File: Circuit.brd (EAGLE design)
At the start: 99 x 72.1 mm, 115 parts, among them IC1 LM1117T-3.3-V, P1 RASPI-P1RASPI_REV2_P1, P5 RASPI_P5

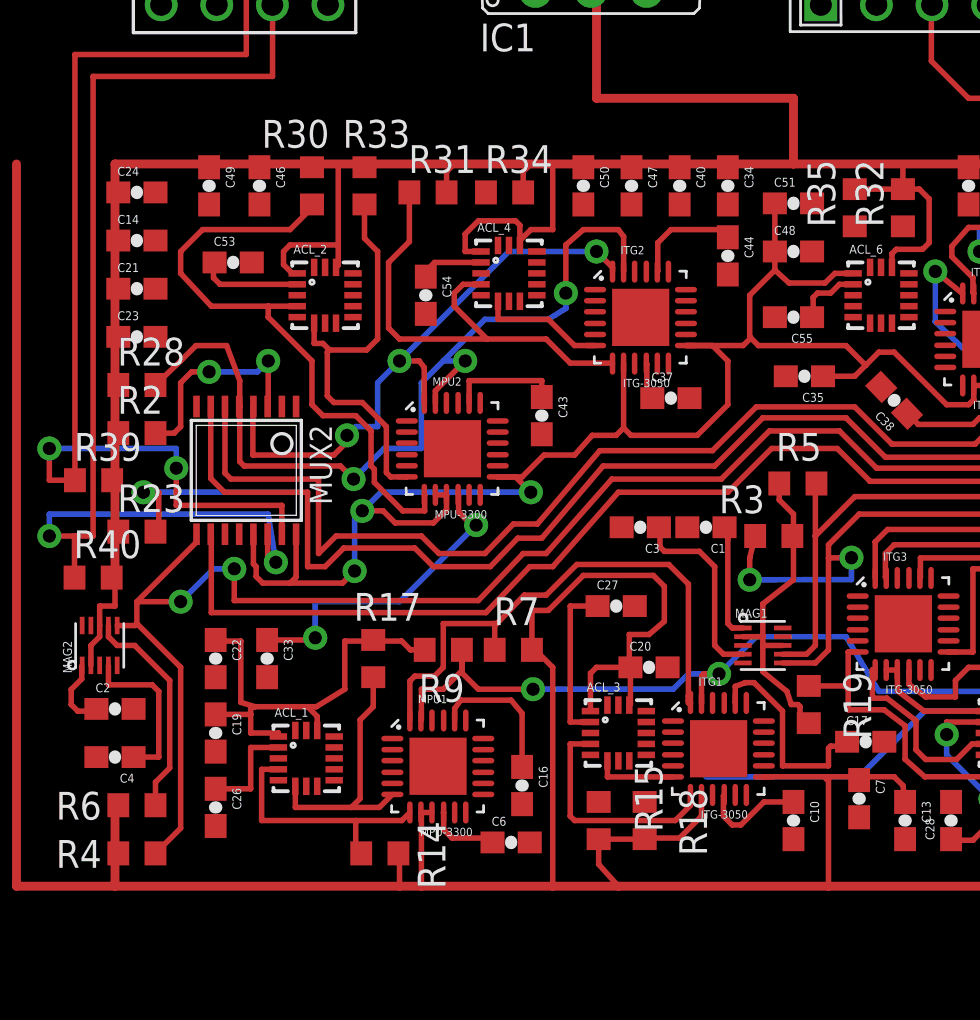
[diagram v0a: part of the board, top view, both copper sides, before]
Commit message: Sorting out missing connections
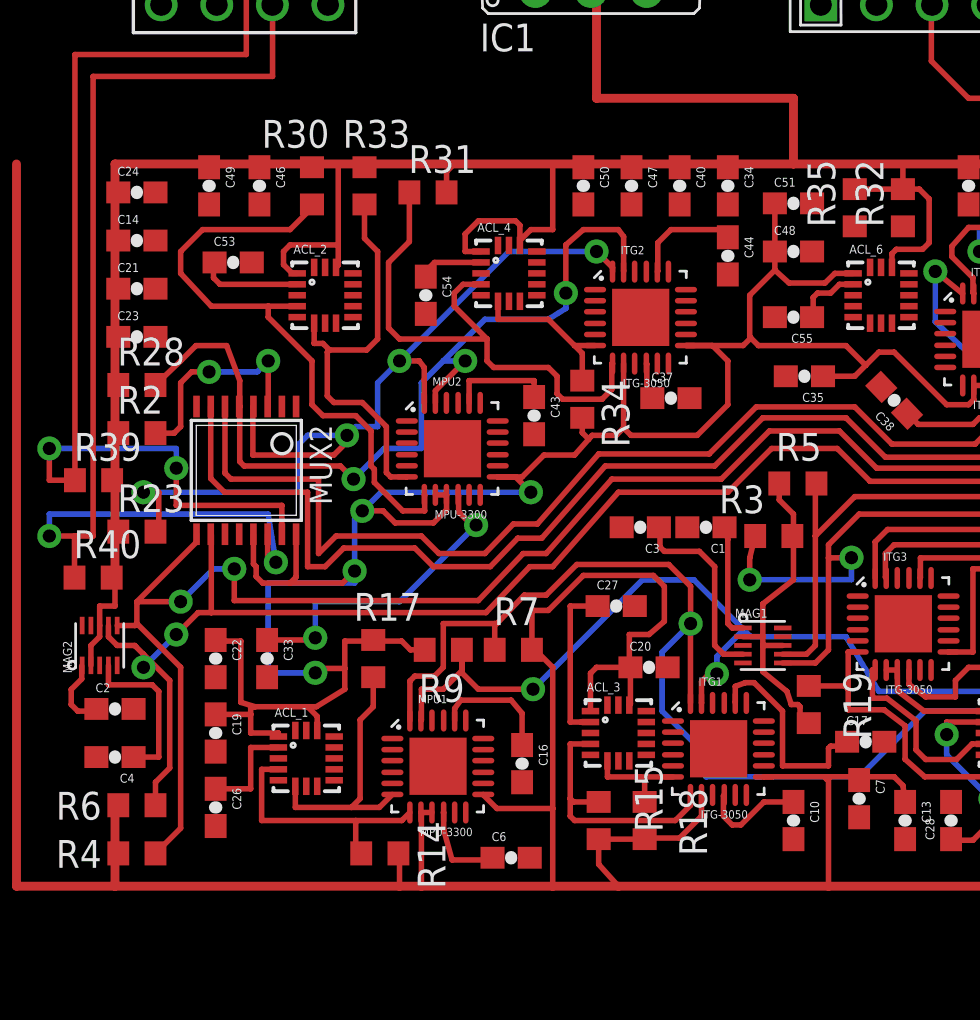
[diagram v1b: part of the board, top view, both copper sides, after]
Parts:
- moved R34 10.1 mm to (51.4, 29.2), turned to 270 degrees
- moved C16 1.00 mm to (48.6, 12.6)
- moved C6 0.70 mm to (48.1, 8.30)
- moved C43 0.35 mm to (49.1, 28.5)
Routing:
- net +3V3: track 661.3 -> 676.7 mm, vias 3 -> 4
- net B1_SD0: track 68.4 -> 76.2 mm, vias 1 -> 2
- net B2_SC2: track 86.9 -> 91.6 mm, vias 2 -> 4
- net B2_SD0: track 36.9 -> 41.5 mm
- net B1_SC0: track 58.3 -> 62.7 mm
- net I2_AUXCLK: track 21.6 -> 24.7 mm
- net I2_AUXSDA: track 5.75 -> 7.50 mm
- net I1_AUXCLK: track 10.6 -> 11.9 mm
- net I1_AUXSDA: track 3.73 -> 4.95 mm
- net N$1: track 6.55 -> 5.55 mm
- net N$2: track 3.25 -> 4.10 mm

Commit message: Slowly does it
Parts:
- moved R35 2.80 mm to (66.6, 38.0)
- moved R32 2.20 mm to (63.8, 38.0)
- moved C17 1.60 mm to (63.0, 12.6), turned to 180 degrees
- moved C41 1.55 mm to (70.5, 39.0)
- moved C55 1.52 mm to (59.5, 32.8)
- moved C10 1.41 mm to (60.0, 9.00)
- moved R5 1.03 mm to (60.5, 24.6)
- moved C7 1.00 mm to (64.0, 10.0)
- moved R3 0.70 mm to (60.1, 22.3)
- moved C48 0.60 mm to (60.4, 36.0)
- moved C38 0.35 mm to (65.3, 28.9), turned to 135.2 degrees
- moved C44 0.35 mm to (57.6, 35.8)
- moved C35 0.18 mm to (61.4, 30.2)
- moved ACL_6 0.15 mm to (64.8, 34.0)
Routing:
- net +3V3: track 676.7 -> 702.8 mm, vias 4 -> 5
- net I4_AUXCLK: track 0.00 -> 14.4 mm
- net I4_AUXSDA: track 0.00 -> 11.2 mm
- net B2_SD1: track 91.0 -> 99.1 mm
- net N$30: track 2.99 -> 7.14 mm, vias 0 -> 2
- net N$4: track 0.00 -> 3.03 mm
- net N$13: track 4.78 -> 3.33 mm
- net B1_SD0: track 76.2 -> 77.3 mm
- net N$34: track 5.93 -> 6.72 mm
- net N$14: track 9.98 -> 9.29 mm
- net B2_SC1: track 87.9 -> 88.5 mm

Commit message: Pause before Skins. I think I've got all airwires?
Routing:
- net +3V3: track 702.8 -> 691.9 mm
- net N$4: track 3.03 -> 0.00 mm
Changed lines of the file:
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@@
 <wire x1="93" y1="29" x2="93" y2="39" width="0.254" layer="1"/>
 <wire x1="93" y1="39" x2="93" y2="40" width="0.254" layer="1"/>
-<wire x1="93" y1="40" x2="77" y2="40" width="0.254" layer="1"/>
 <wire x1="76.6" y1="40" x2="75" y2="40" width="0.254" layer="1"/>
 <wire x1="75" y1="40" x2="70.25" y2="40" width="0.254" layer="1"/>
@@
 <wire x1="29.85" y1="21.1" x2="30.1" y2="20.9" width="0.254" layer="1"/>
 <wire x1="30.1" y1="20.9" x2="30" y2="21" width="0.254" layer="1"/>
-<wire x1="93" y1="40" x2="70.25" y2="40" width="0.4064" layer="1"/>
+<wire x1="93" y1="40" x2="77" y2="40" width="0.4064" layer="1"/>
+<wire x1="77" y1="40" x2="70.25" y2="40" width="0.4064" layer="1"/>
 <wire x1="70.25" y1="40" x2="63.8" y2="40" width="0.4064" layer="1"/>
 <wire x1="63.8" y1="40" x2="61" y2="40" width="0.4064" layer="1"/>
@@
 <wire x1="72.75" y1="27.9" x2="72.75" y2="26.75" width="0.254" layer="16"/>
 <wire x1="72.75" y1="26.75" x2="72" y2="26" width="0.254" layer="16"/>
+<wire x1="77" y1="40" x2="80.25" y2="40" width="0.254" layer="1"/>
+<wire x1="80.25" y1="40" x2="81.55" y2="38.7" width="0.254" layer="1"/>
 <wire x1="89" y1="39" x2="89" y2="38.85" width="0" layer="19" extent="1-1"/>
 <wire x1="34.75" y1="18.25" x2="34.6" y2="18.25" width="0" layer="19" extent="1-1"/>
-<wire x1="74" y1="30" x2="72.55" y2="30.7033" width="0" layer="19" extent="1-1"/>
 <wire x1="36.6" y1="39.85" x2="34.3" y2="39.85" width="0" layer="19" extent="1-1"/>
 </signal>
@@
 </signal>
 <signal name="N$4">
-<wire x1="81.5" y1="39.9" x2="81.45" y2="39.95" width="0.254" layer="1"/>
-<wire x1="81.5" y1="38.65" x2="81.5" y2="39.5" width="0.254" layer="1"/>
-<wire x1="81.5" y1="39.5" x2="81.1" y2="39.9" width="0.254" layer="1"/>
-<wire x1="82" y1="40" x2="81" y2="40" width="0.254" layer="1"/>
-<wire x1="81.5" y1="39.9" x2="81.1" y2="39.9" width="0.254" layer="1"/>
-<wire x1="81.1" y1="39.9" x2="81" y2="40" width="0.254" layer="1"/>
 </signal>
 </signals>

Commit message: Before pouring copper
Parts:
- moved IC1 22.8 mm to (29.8, 45.2)
- moved P1 22.8 mm to (72.0, 40.0)
- moved P5 22.8 mm to (19.0, 40.0)
- moved C9 22.4 mm to (57.4, 15.6)
- moved C36 22.4 mm to (60.4, 31.8)
- moved R10 22.4 mm to (58.4, 12.0)
- moved R11 22.4 mm to (57.4, 6.20)
- moved R26 22.4 mm to (55.9, 32.2)
- moved ACL_1 22.4 mm to (16.7, 8.84)
- moved C33 22.4 mm to (14.9, 13.4)
- moved C5 22.4 mm to (55.3, 15.6)
- moved C54 22.4 mm to (22.2, 30.0)
- moved C6 22.4 mm to (26.1, 4.30)
- moved MPU1 22.4 mm to (22.7, 8.49)
- moved R7 22.4 mm to (26.2, 13.8)
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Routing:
- net +3V3: track 691.9 -> 828.0 mm
- net SDA2: track 50.4 -> 48.4 mm
- net SDA1: track 59.1 -> 57.1 mm
- net CLK2: track 51.3 -> 49.3 mm
- net CLK1: track 61.1 -> 59.1 mm
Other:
- board size 99 x 72.1 mm -> 78 x 49.1 mm

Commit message: Adding wires for grounds
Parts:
- moved C16 0.10 mm to (26.7, 8.60)
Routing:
- net GND: track 3.90 -> 197.0 mm, vias 0 -> 2
- net +3V3: track 828.0 -> 820.8 mm
- net N$41: track 0.00 -> 3.49 mm
- net B2_SC2: track 91.6 -> 90.9 mm

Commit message: Going home now!
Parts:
- moved R23 24.7 mm to (29.2, 33.3)
- moved R5 2.56 mm to (41.1, 20.4)
- moved R39 2.45 mm to (6.00, 23.8), turned to 270 degrees
- moved R38 2.35 mm to (69.2, 25.4)
- moved C52 2.30 mm to (66.8, 25.4), turned to 90 degrees
- moved R2 2.20 mm to (9.00, 25.9)
- moved R28 2.20 mm to (9.00, 23.7)
- moved C2 2.05 mm to (5.95, 11.1)
- moved C56 2.00 mm to (69.0, 34.0), turned to 180 degrees
- moved MAG1 1.75 mm to (37.6, 15.8)
- moved C27 1.56 mm to (29.8, 14.8), turned to 90 degrees
- moved C6 1.55 mm to (24.6, 4.30)
- moved C58 1.36 mm to (68.1, 28.0), turned to 0 degrees
- moved C16 1.00 mm to (26.7, 9.60)
- moved C34 1.00 mm to (36.0, 36.0)
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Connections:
- removed net MAG1_INT: MAG1.9
- removed net MAG2_INT: MAG2.9
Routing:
- net +3V3: track 820.8 -> 764.1 mm, vias 5 -> 6
- net GND: track 197.0 -> 214.8 mm, vias 2 -> 12
- net B2_SD2: track 96.1 -> 85.6 mm, vias 4 -> 2
- net B2_SC2: track 90.9 -> 83.5 mm, vias 4 -> 2
- net B1_SD2: track 52.7 -> 46.9 mm
- net B1_SC2: track 50.9 -> 45.8 mm
- net SDA2: track 48.4 -> 44.9 mm
- net N$50: track 9.13 -> 5.73 mm
- net M1_AUXSDA: track 12.0 -> 15.2 mm
- net M1_AUXCLK: track 11.8 -> 14.9 mm
- net B2_SC0: track 40.6 -> 43.7 mm
- net I2_AUXCLK: track 24.7 -> 22.1 mm
- net N$23: track 9.31 -> 11.7 mm
- net CLK2: track 49.3 -> 51.7 mm
- net N$49: track 7.46 -> 5.23 mm
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- added copper zone on layer 1, net GND
- added copper zone on layer 16, net GND

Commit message: Stashing for safety
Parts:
- moved R7 4.05 mm to (29.9, 15.6)
- moved C17 2.47 mm to (40.3, 11.0), turned to 0 degrees
- moved R19 2.25 mm to (39.8, 13.4), turned to 180 degrees
- moved C27 2.09 mm to (28.3, 13.2), turned to 180 degrees
- moved R3 1.86 mm to (39.9, 18.1), turned to 180 degrees
- moved C10 1.39 mm to (36.7, 4.50), turned to 0 degrees
- moved C20 1.01 mm to (31.5, 13.2)
- moved ACL_3 1.00 mm to (30.0, 10.0)
- moved C13 0.55 mm to (44.1, 5.45)
- moved C28 0.55 mm to (46.2, 5.45)
- moved C7 0.55 mm to (42.0, 5.45)
- moved R14 0.25 mm to (20.0, 4.25)
- moved R34 0.20 mm to (29.6, 25.2)
- moved C16 0.16 mm to (26.6, 9.65)
- moved C5 0.11 mm to (55.2, 15.5)
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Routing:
- net GND: track 214.8 -> 187.4 mm
- net +3V3: track 764.1 -> 742.4 mm
- net B1_SD0: track 78.6 -> 69.2 mm
- net B1_SD1: track 41.5 -> 36.0 mm
- net N$14: track 9.87 -> 4.60 mm
- net B1_SD2: track 46.9 -> 42.2 mm, vias 4 -> 2
- net I1_AUXSDA: track 5.95 -> 7.59 mm
- net B1_SC0: track 62.2 -> 60.6 mm
- net M2_AUXSDA: track 18.5 -> 17.1 mm
- net B1_SC2: track 45.8 -> 47.2 mm
- net N$9: track 5.70 -> 4.67 mm
- net B1_SC1: track 41.6 -> 40.6 mm
- net I2_AUXCLK: track 22.1 -> 21.3 mm
- net M1_AUXCLK: track 14.9 -> 14.3 mm
- net N$13: track 3.33 -> 2.70 mm
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
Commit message: Going home again!
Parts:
- moved C45 14.1 mm to (49.9, 31.6)
- moved R16 9.74 mm to (41.8, 10.5)
- moved C28 8.48 mm to (49.4, 13.3), turned to 0 degrees
- moved C11 5.27 mm to (45.5, 10.5), turned to 90 degrees
- moved C18 4.25 mm to (48.7, 17.1)
- moved C52 4.25 mm to (70.0, 28.2), turned to 180 degrees
- moved R22 4.00 mm to (72.0, 9.35), turned to 180 degrees
- moved C36 3.39 mm to (62.5, 34.5), turned to 0 degrees
- moved R10 3.06 mm to (60.3, 14.4)
- moved C35 2.96 mm to (37.1, 26.4)
- moved C58 2.91 mm to (66.8, 25.4), turned to 270 degrees
- moved R29 2.82 mm to (50.8, 35.0), turned to 270 degrees
- moved C51 2.35 mm to (38.9, 36.5)
- moved C31 2.30 mm to (67.9, 9.35), turned to 0 degrees
- moved C8 1.70 mm to (50.8, 17.1), turned to 270 degrees
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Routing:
- net GND: track 187.4 -> 121.9 mm, vias 12 -> 8
- net N$35: track 20.1 -> 1.61 mm, vias 2 -> 0
- net B2_SC1: track 87.3 -> 71.5 mm
- net +3V3: track 742.4 -> 755.2 mm, vias 6 -> 17
- net B2_SD0: track 41.2 -> 29.0 mm, vias 4 -> 3
- net B2_SC2: track 83.5 -> 95.3 mm, vias 2 -> 4
- net N$23: track 12.2 -> 3.96 mm, vias 2 -> 0
- net B1_SD1: track 36.0 -> 43.0 mm
- net I3_AUXSDA: track 13.1 -> 18.7 mm, vias 0 -> 2
- net N$28: track 10.6 -> 5.08 mm
- net N$30: track 7.21 -> 12.1 mm
- net B2_SD1: track 97.8 -> 93.4 mm
- net I4_AUXCLK: track 14.2 -> 18.6 mm, vias 0 -> 2
- net B2_SD2: track 85.6 -> 89.6 mm
- net N$27: track 7.26 -> 4.21 mm
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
